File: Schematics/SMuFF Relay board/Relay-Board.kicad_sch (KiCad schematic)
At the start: 13 parts

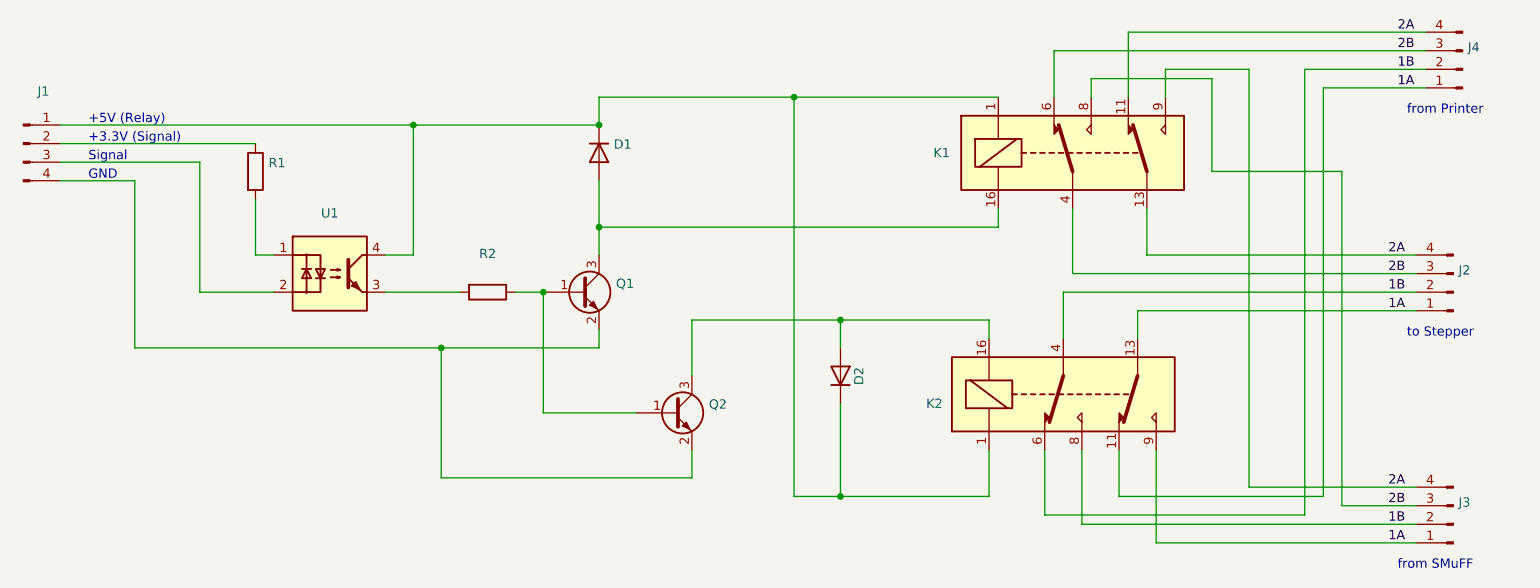
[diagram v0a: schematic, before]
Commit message: Updated for arduino framework 2.4.0
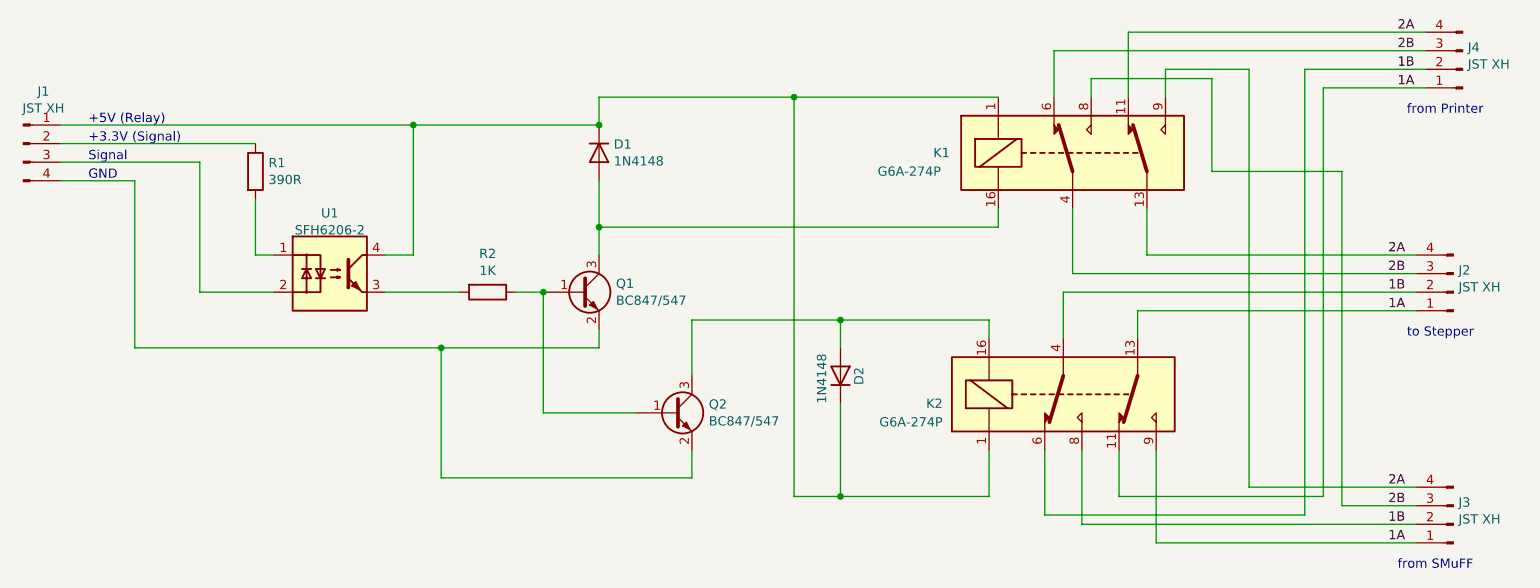
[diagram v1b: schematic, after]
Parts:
- D1, D2: value (none) -> 1N4148
- J1, J2, J3, J4: value (none) -> JST XH; footprint (none) -> Connector_JST:JST_XH_B4B-XH-A_1x04_P2.50mm_Vertical
- K1, K2: value (none) -> G6A-274P; footprint (none) -> Relay_THT:Relay_DPDT_Omron_G5V-2
- Q1, Q2: value (none) -> BC847/547; footprint (none) -> Package_TO_SOT_SMD:SOT-23
- R1: value (none) -> 390R; footprint (none) -> Resistor_SMD:R_0603_1608Metric
- R2: value (none) -> 1K; footprint (none) -> Resistor_SMD:R_0603_1608Metric
- U1: value (none) -> SFH6206-2; footprint (none) -> Package_DIP:SMDIP-4_W9.53mm_Clearance8mm
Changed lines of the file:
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@@
     (title "SMuFF Mini Relay Board")
     (date "2020-12-06")
-    (rev "1")
+    (rev "2")
     (company "Technik Gegg")
     (comment 3 "AISLER Project ID: FMWPPUGV")
@@
     (in_bom yes) (on_board yes)
     (property "Reference" "U1" (id 0) (at 83.82 84.455 0))
-    (property "Value" "" (id 1) (at 83.82 86.7664 0))
-    (property "Footprint" "" (id 2) (at 78.74 97.79 0)
+    (property "Value" "SFH6206-2" (id 1) (at 83.82 86.7664 0))
+    (property "Footprint" "Package_DIP:SMDIP-4_W9.53mm_Clearance8mm" (id 2) (at 78.74 97.79 0)
       (effects (font (size 1.27 1.27) italic) (justify left) hide)
     )
@@
       (effects (font (size 1.27 1.27)) (justify left))
     )
-    (property "Value" "" (id 1) (at 75.438 79.883 0)
-      (effects (font (size 1.27 1.27)) (justify left))
-    )
-    (property "Footprint" "" (id 2) (at 71.882 78.74 90)
+    (property "Value" "390R" (id 1) (at 75.438 79.883 0)
+      (effects (font (size 1.27 1.27)) (justify left))
+    )
+    (property "Footprint" "Resistor_SMD:R_0603_1608Metric" (id 2) (at 71.882 78.74 90)
       (effects (font (size 1.27 1.27)) hide)
     )
@@
     (in_bom yes) (on_board yes)
     (property "Reference" "R2" (id 0) (at 105.41 89.9922 90))
-    (property "Value" "" (id 1) (at 105.41 92.3036 90))
-    (property "Footprint" "" (id 2) (at 105.41 93.472 90)
+    (property "Value" "1K" (id 1) (at 105.41 92.3036 90))
+    (property "Footprint" "Resistor_SMD:R_0603_1608Metric" (id 2) (at 105.41 93.472 90)
       (effects (font (size 1.27 1.27)) hide)
     )
@@
       (effects (font (size 1.27 1.27)) (justify left))
     )
-    (property "Value" "" (id 1) (at 122.9614 96.393 0)
-      (effects (font (size 1.27 1.27)) (justify left))
-    )
-    (property "Footprint" "" (id 2) (at 123.19 97.155 0)
+    (property "Value" "BC847/547" (id 1) (at 122.9614 96.393 0)
+      (effects (font (size 1.27 1.27)) (justify left))
+    )
+    (property "Footprint" "Package_TO_SOT_SMD:SOT-23" (id 2) (at 123.19 97.155 0)
       (effects (font (size 1.27 1.27) italic) (justify left) hide)
     )
@@
       (effects (font (size 1.27 1.27)) (justify left))
     )
-    (property "Value" "" (id 1) (at 135.6614 112.903 0)
-      (effects (font (size 1.27 1.27)) (justify left))
-    )
-    (property "Footprint" "" (id 2) (at 135.89 113.665 0)
+    (property "Value" "BC847/547" (id 1) (at 135.6614 112.903 0)
+      (effects (font (size 1.27 1.27)) (justify left))
+    )
+    (property "Footprint" "Package_TO_SOT_SMD:SOT-23" (id 2) (at 135.89 113.665 0)
       (effects (font (size 1.27 1.27) italic) (justify left) hide)
     )
@@
       (effects (font (size 1.27 1.27)) (justify left))
     )
-    (property "Value" "" (id 1) (at 122.6566 77.343 90)
+    (property "Value" "1N4148" (id 1) (at 122.6566 77.343 90)
       (effects (font (size 1.27 1.27)) (justify left))
     )
@@
       (effects (font (size 1.27 1.27)) (justify left))
     )
-    (property "Value" "" (id 1) (at 151.13 110.49 0)
+    (property "Value" "1N4148" (id 1) (at 151.13 110.49 0)
       (effects (font (size 1.27 1.27)) (justify left))
     )
@@
     (in_bom yes) (on_board yes)
     (property "Reference" "J1" (id 0) (at 44.6532 67.7926 0))
-    (property "Value" "" (id 1) (at 44.6532 70.104 0))
-    (property "Footprint" "" (id 2) (at 41.91 74.93 0)
+    (property "Value" "JST XH" (id 1) (at 44.6532 70.104 0))
+    (property "Footprint" "Connector_JST:JST_XH_B4B-XH-A_1x04_P2.50mm_Vertical" (id 2) (at 41.91 74.93 0)
       (effects (font (size 1.27 1.27)) hide)
     )
@@
       (effects (font (size 1.27 1.27)) (justify right))
     )
-    (property "Value" "" (id 1) (at 239.4712 64.0842 0)
-      (effects (font (size 1.27 1.27)) (justify right))
-    )
-    (property "Footprint" "" (id 2) (at 238.76 64.77 0)
+    (property "Value" "JST XH" (id 1) (at 239.4712 64.0842 0)
+      (effects (font (size 1.27 1.27)) (justify right))
+    )
+    (property "Footprint" "Connector_JST:JST_XH_B4B-XH-A_1x04_P2.50mm_Vertical" (id 2) (at 238.76 64.77 0)
       (effects (font (size 1.27 1.27)) hide)
     )
@@
       (effects (font (size 1.27 1.27)) (justify right))
     )
-    (property "Value" "" (id 1) (at 238.2012 94.5642 0)
-      (effects (font (size 1.27 1.27)) (justify right))
-    )
-    (property "Footprint" "" (id 2) (at 237.49 95.25 0)
+    (property "Value" "JST XH" (id 1) (at 238.2012 94.5642 0)
+      (effects (font (size 1.27 1.27)) (justify right))
+    )
+    (property "Footprint" "Connector_JST:JST_XH_B4B-XH-A_1x04_P2.50mm_Vertical" (id 2) (at 237.49 95.25 0)
       (effects (font (size 1.27 1.27)) hide)
     )
@@
       (effects (font (size 1.27 1.27)) (justify right))
     )
-    (property "Value" "" (id 1) (at 238.2012 126.3142 0)
-      (effects (font (size 1.27 1.27)) (justify right))
-    )
-    (property "Footprint" "" (id 2) (at 237.49 127 0)
+    (property "Value" "JST XH" (id 1) (at 238.2012 126.3142 0)
+      (effects (font (size 1.27 1.27)) (justify right))
+    )
+    (property "Footprint" "Connector_JST:JST_XH_B4B-XH-A_1x04_P2.50mm_Vertical" (id 2) (at 237.49 127 0)
       (effects (font (size 1.27 1.27)) hide)
     )
@@
       (effects (font (size 1.27 1.27)) (justify left))
     )
-    (property "Value" "" (id 1) (at 158.75 78.74 0)
-      (effects (font (size 1.27 1.27)) (justify left))
-    )
-    (property "Footprint" "" (id 2) (at 201.93 77.47 0)
+    (property "Value" "G6A-274P" (id 1) (at 158.75 78.74 0)
+      (effects (font (size 1.27 1.27)) (justify left))
+    )
+    (property "Footprint" "Relay_THT:Relay_DPDT_Omron_G5V-2" (id 2) (at 201.93 77.47 0)
       (effects (font (size 1.27 1.27)) (justify left) hide)
     )
@@
       (effects (font (size 1.27 1.27)) (justify right))
     )
-    (property "Value" "" (id 1) (at 167.64 113.03 0)
-      (effects (font (size 1.27 1.27)) (justify right))
-    )
-    (property "Footprint" "" (id 2) (at 200.66 107.95 0)
+    (property "Value" "G6A-274P" (id 1) (at 167.64 113.03 0)
+      (effects (font (size 1.27 1.27)) (justify right))
+    )
+    (property "Footprint" "Relay_THT:Relay_DPDT_Omron_G5V-2" (id 2) (at 200.66 107.95 0)
       (effects (font (size 1.27 1.27)) (justify left) hide)
     )
@@
   (symbol_instances
     (path "/00000000-0000-0000-0000-00005fccc4a8"
-      (reference "D1") (unit 1) (value "1N4148") (footprint "Diode_SMD:D_0603_1608Metric")
+      (reference "D1") (unit 1) (value "1N4148") (footprint "Diode_SMD:D_SOD-123")
     )
     (path "/00000000-0000-0000-0000-00005fccde35"
-      (reference "D2") (unit 1) (value "1N4148") (footprint "Diode_SMD:D_0603_1608Metric")
+      (reference "D2") (unit 1) (value "1N4148") (footprint "Diode_SMD:D_SOD-123")
     )
     (path "/00000000-0000-0000-0000-00005fcd4c35"
